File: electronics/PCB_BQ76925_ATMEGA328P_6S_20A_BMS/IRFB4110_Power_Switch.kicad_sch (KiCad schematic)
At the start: 25 parts, among them Q1 IRFB4110, Q2 IRFB4110, Q3 IRFB4110, Q4 IRFB4110, Q5 BC817, U2 LMR50410

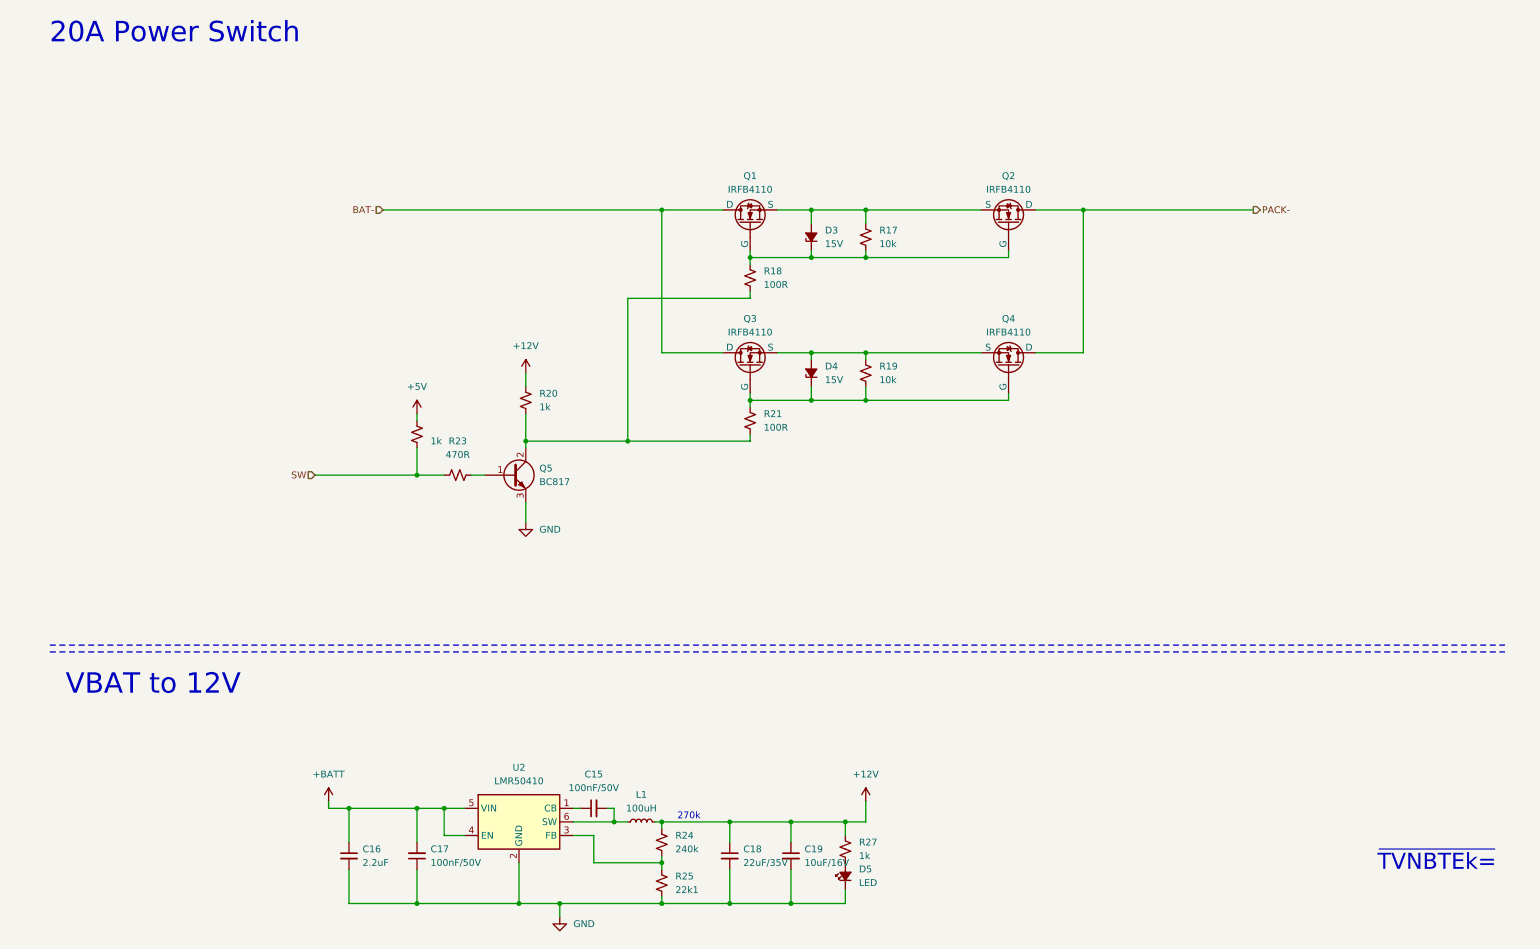
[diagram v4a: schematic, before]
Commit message: schematic components footprint updated
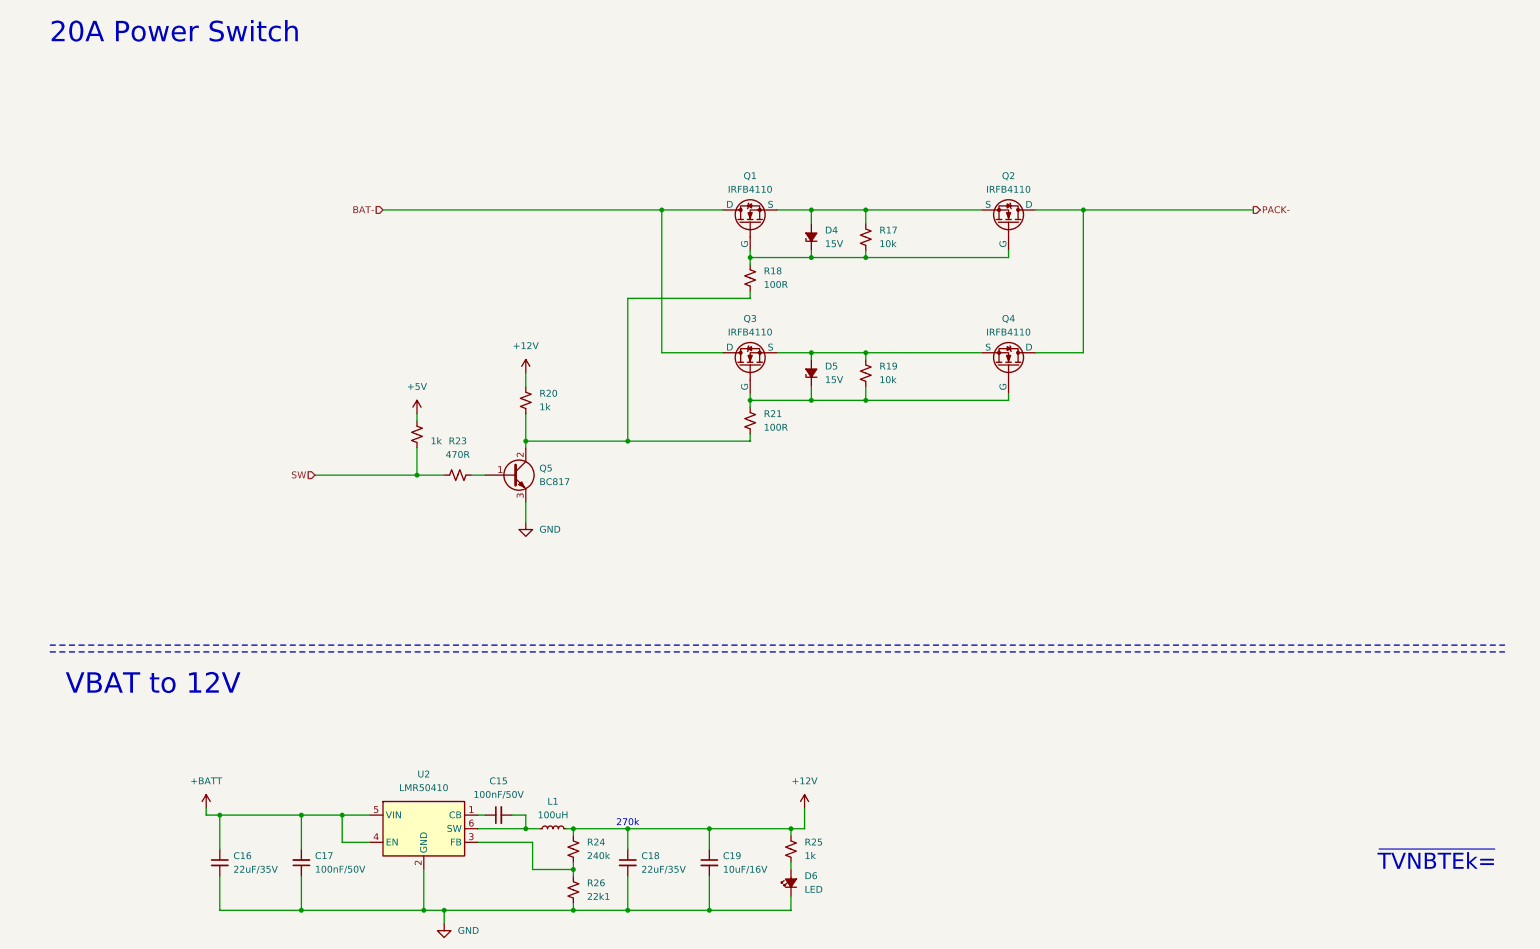
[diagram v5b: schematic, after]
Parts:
- removed Q1, Q2, Q3, Q4: IRFB4110, symbol BQ76925_ATMEGA328P_6S_20A_BMS:NMOS_1
- added Q1, Q2, Q3, Q4: IRFB4110, Package_TO_SOT_THT:TO-220-3_Horizontal_TabDown, symbol BQ76925_ATMEGA328P_6S_20A_BMS:NMOS
- C16: value 2.2uF -> 22uF/35V; footprint (none) -> Capacitor_SMD:CP_Elec_6.3x5.7
- D4: renamed from D3; footprint (none) -> Diode_SMD:D_SOD-123
- D5: renamed from D4; footprint (none) -> Diode_SMD:D_SOD-123
- D6: renamed from D5; symbol Device:LED_Small_Filled -> BQ76925_ATMEGA328P_6S_20A_BMS:LED_Small_Filled
- renumbered R27 to R25, R25 to R26
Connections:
- net BAT-: now also Q1.2 (D), Q3.2 (D)
- net PACK-: now also Q2.2 (D), Q4.2 (D)
- net at D4.1 (K), R17.1, R18.1: now also Q1.1 (G), Q2.1 (G)
- net at D4.2 (A), R17.2: now also Q1.3 (S), Q2.3 (S)
- net at D5.1 (K), R19.1, R21.1: now also Q3.1 (G), Q4.1 (G)
- net at D5.2 (A), R19.2: now also Q3.3 (S), Q4.3 (S)
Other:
- moved on the sheet: C15, C17, C18, C19, D6, L1, R24, R25, R26, U2

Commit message: pcb design half complete
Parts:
- added C18: 100nF/50V, Capacitor_SMD:C_0805_2012Metric_Pad1.18x1.45mm_HandSolder, symbol BQ76925_ATMEGA328P_6S_20A_BMS:C_Small
- renumbered C16 to C15, C17 to C16, C15 to C17, C18 to C19, C19 to C20, D6 to D4, D4 to D5, D5 to D6, Q5 to Q1, Q1 to Q2, Q2 to Q4, Q4 to Q5, R22 to R17, R23 to R18, R20 to R19, R24 to R20, R26 to R21, R18 to R22, R21 to R23, R25 to R24, R17 to R25, R19 to R26
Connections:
- net GND: now also C18.2
- net at Q1.2 (C), R19.1, R22.2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: now also C18.1

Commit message: PCB DRC complete footprints library exported. PCB optimization required
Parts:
- C15, C19: footprint Capacitor_SMD:CP_Elec_6.3x5.7 -> BQ76925_ATMEGA328P_6S_20A_BMS:CP_Elec_6.3x5.7
- C16, C17, C18: footprint Capacitor_SMD:C_0805_2012Metric_Pad1.18x1.45mm_HandSolder -> BQ76925_ATMEGA328P_6S_20A_BMS:C_0805_2012Metric_Pad1.18x1.45mm_HandSolder
- C20: footprint Capacitor_SMD:C_0603_1608Metric_Pad1.08x0.95mm_HandSolder -> BQ76925_ATMEGA328P_6S_20A_BMS:C_0603_1608Metric_Pad1.08x0.95mm_HandSolder
- D4, R20: footprint Resistor_SMD:R_0805_2012Metric_Pad1.20x1.40mm_HandSolder -> BQ76925_ATMEGA328P_6S_20A_BMS:R_0805_2012Metric_Pad1.20x1.40mm_HandSolder
- D5, D6: footprint Diode_SMD:D_SOD-123 -> BQ76925_ATMEGA328P_6S_20A_BMS:D_SOD-123
- L1: footprint Inductor_SMD:L_7.3x7.3_H3.5 -> BQ76925_ATMEGA328P_6S_20A_BMS:L_7.3x7.3_H3.5
- Q1: footprint Package_TO_SOT_SMD:SOT-23 -> BQ76925_ATMEGA328P_6S_20A_BMS:SOT-23
- Q2, Q3, Q4, Q5: footprint Package_TO_SOT_THT:TO-220-3_Horizontal_TabDown -> BQ76925_ATMEGA328P_6S_20A_BMS:TO-220-3_Horizontal_TabDown
- R17, R18, R19, R21, R24, R25, R26: footprint Resistor_SMD:R_0603_1608Metric_Pad0.98x0.95mm_HandSolder -> BQ76925_ATMEGA328P_6S_20A_BMS:R_0603_1608Metric_Pad0.98x0.95mm_HandSolder
- R22, R23: footprint Resistor_SMD:R_1206_3216Metric_Pad1.30x1.75mm_HandSolder -> BQ76925_ATMEGA328P_6S_20A_BMS:R_1206_3216Metric_Pad1.30x1.75mm_HandSolder
- U2: footprint Package_TO_SOT_SMD:SOT-23-6 -> BQ76925_ATMEGA328P_6S_20A_BMS:SOT-23-6
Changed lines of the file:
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@@
 			)
 		)
-		(property "Footprint" "Capacitor_SMD:C_0805_2012Metric_Pad1.18x1.45mm_HandSolder"
+		(property "Footprint" "BQ76925_ATMEGA328P_6S_20A_BMS:C_0805_2012Metric_Pad1.18x1.45mm_HandSolder"
 			(at 59.69 173.99 0)
 			(effects
@@
 			)
 		)
-		(property "Footprint" "Package_TO_SOT_THT:TO-220-3_Horizontal_TabDown"
+		(property "Footprint" "BQ76925_ATMEGA328P_6S_20A_BMS:TO-220-3_Horizontal_TabDown"
 			(at 200.406 77.216 0)
 			(effects
@@
 			)
 		)
-		(property "Footprint" "Capacitor_SMD:C_0805_2012Metric_Pad1.18x1.45mm_HandSolder"
+		(property "Footprint" "BQ76925_ATMEGA328P_6S_20A_BMS:C_0805_2012Metric_Pad1.18x1.45mm_HandSolder"
 			(at 96.52 165.1 0)
 			(effects
@@
 			)
 		)
-		(property "Footprint" "Package_TO_SOT_THT:TO-220-3_Horizontal_TabDown"
+		(property "Footprint" "BQ76925_ATMEGA328P_6S_20A_BMS:TO-220-3_Horizontal_TabDown"
 			(at 134.874 77.216 0)
 			(effects
@@
 			)
 		)
-		(property "Footprint" "Resistor_SMD:R_0603_1608Metric_Pad0.98x0.95mm_HandSolder"
+		(property "Footprint" "BQ76925_ATMEGA328P_6S_20A_BMS:R_0603_1608Metric_Pad0.98x0.95mm_HandSolder"
 			(at 110.49 179.07 0)
 			(effects
@@
 			)
 		)
-		(property "Footprint" "Resistor_SMD:R_0603_1608Metric_Pad0.98x0.95mm_HandSolder"
+		(property "Footprint" "BQ76925_ATMEGA328P_6S_20A_BMS:R_0603_1608Metric_Pad0.98x0.95mm_HandSolder"
 			(at 165.1 82.55 0)
 			(effects
@@
 			)
 		)
-		(property "Footprint" "Resistor_SMD:R_0805_2012Metric_Pad1.20x1.40mm_HandSolder"
+		(property "Footprint" "BQ76925_ATMEGA328P_6S_20A_BMS:R_0805_2012Metric_Pad1.20x1.40mm_HandSolder"
 			(at 110.49 171.45 0)
 			(effects
@@
 			)
 		)
-		(property "Footprint" "Capacitor_SMD:C_0603_1608Metric_Pad1.08x0.95mm_HandSolder"
+		(property "Footprint" "BQ76925_ATMEGA328P_6S_20A_BMS:C_0603_1608Metric_Pad1.08x0.95mm_HandSolder"
 			(at 135.89 173.99 0)
 			(effects
@@
 			)
 		)
-		(property "Footprint" "Resistor_SMD:R_0603_1608Metric_Pad0.98x0.95mm_HandSolder"
+		(property "Footprint" "BQ76925_ATMEGA328P_6S_20A_BMS:R_0603_1608Metric_Pad0.98x0.95mm_HandSolder"
 			(at 151.13 171.45 0)
 			(effects
@@
 			)
 		)
-		(property "Footprint" "Diode_SMD:D_SOD-123"
+		(property "Footprint" "BQ76925_ATMEGA328P_6S_20A_BMS:D_SOD-123"
 			(at 154.94 82.55 90)
 			(effects
@@
 			)
 		)
-		(property "Footprint" "Capacitor_SMD:C_0805_2012Metric_Pad1.18x1.45mm_HandSolder"
+		(property "Footprint" "BQ76925_ATMEGA328P_6S_20A_BMS:C_0805_2012Metric_Pad1.18x1.45mm_HandSolder"
 			(at 115.57 102.87 0)
 			(effects
@@
 			)
 		)
-		(property "Footprint" "Package_TO_SOT_SMD:SOT-23"
+		(property "Footprint" "BQ76925_ATMEGA328P_6S_20A_BMS:SOT-23"
 			(at 104.14 99.06 0)
 			(effects
@@
 			)
 		)
-		(property "Footprint" "Resistor_SMD:R_0603_1608Metric_Pad0.98x0.95mm_HandSolder"
+		(property "Footprint" "BQ76925_ATMEGA328P_6S_20A_BMS:R_0603_1608Metric_Pad0.98x0.95mm_HandSolder"
 			(at 81.28 93.98 0)
 			(effects
@@
 			)
 		)
-		(property "Footprint" "Package_TO_SOT_SMD:SOT-23-6"
+		(property "Footprint" "BQ76925_ATMEGA328P_6S_20A_BMS:SOT-23-6"
 			(at 83.82 176.53 0)
 			(effects
@@
 			)
 		)
-		(property "Footprint" "Resistor_SMD:R_0603_1608Metric_Pad0.98x0.95mm_HandSolder"
+		(property "Footprint" "BQ76925_ATMEGA328P_6S_20A_BMS:R_0603_1608Metric_Pad0.98x0.95mm_HandSolder"
 			(at 165.1 57.15 0)
 			(effects
@@
 			)
 		)
-		(property "Footprint" "Resistor_SMD:R_1206_3216Metric_Pad1.30x1.75mm_HandSolder"
+		(property "Footprint" "BQ76925_ATMEGA328P_6S_20A_BMS:R_1206_3216Metric_Pad1.30x1.75mm_HandSolder"
 			(at 143.51 91.44 0)
 			(effects
@@
 			)
 		)
-		(property "Footprint" "Capacitor_SMD:CP_Elec_6.3x5.7"
+		(property "Footprint" "BQ76925_ATMEGA328P_6S_20A_BMS:CP_Elec_6.3x5.7"
 			(at 44.45 173.99 0)
 			(effects
@@
 			)
 		)
-		(property "Footprint" "Capacitor_SMD:CP_Elec_6.3x5.7"
+		(property "Footprint" "BQ76925_ATMEGA328P_6S_20A_BMS:CP_Elec_6.3x5.7"
 			(at 120.65 173.99 0)
 			(effects
@@
 			)
 		)
-		(property "Footprint" "Package_TO_SOT_THT:TO-220-3_Horizontal_TabDown"
+		(property "Footprint" "BQ76925_ATMEGA328P_6S_20A_BMS:TO-220-3_Horizontal_TabDown"
 			(at 200.406 50.546 0)
 			(effects
@@
 			)
 		)
-		(property "Footprint" "Inductor_SMD:L_7.3x7.3_H3.5"
+		(property "Footprint" "BQ76925_ATMEGA328P_6S_20A_BMS:L_7.3x7.3_H3.5"
 			(at 106.68 167.64 0)
 			(effects
@@
 			)
 		)
-		(property "Footprint" "Diode_SMD:D_SOD-123"
+		(property "Footprint" "BQ76925_ATMEGA328P_6S_20A_BMS:D_SOD-123"
 			(at 154.94 57.15 90)
 			(effects
@@
 			)
 		)
-		(property "Footprint" "Resistor_SMD:R_0805_2012Metric_Pad1.20x1.40mm_HandSolder"
+		(property "Footprint" "BQ76925_ATMEGA328P_6S_20A_BMS:R_0805_2012Metric_Pad1.20x1.40mm_HandSolder"
 			(at 151.13 177.8 90)
 			(effects
@@
 			)
 		)
-		(property "Footprint" "Package_TO_SOT_THT:TO-220-3_Horizontal_TabDown"
+		(property "Footprint" "BQ76925_ATMEGA328P_6S_20A_BMS:TO-220-3_Horizontal_TabDown"
 			(at 134.874 50.546 0)
 			(effects
@@
 			)
 		)
-		(property "Footprint" "Resistor_SMD:R_0603_1608Metric_Pad0.98x0.95mm_HandSolder"
+		(property "Footprint" "BQ76925_ATMEGA328P_6S_20A_BMS:R_0603_1608Metric_Pad0.98x0.95mm_HandSolder"
 			(at 101.6 87.63 0)
 			(effects
@@
 			)
 		)
-		(property "Footprint" "Resistor_SMD:R_1206_3216Metric_Pad1.30x1.75mm_HandSolder"
+		(property "Footprint" "BQ76925_ATMEGA328P_6S_20A_BMS:R_1206_3216Metric_Pad1.30x1.75mm_HandSolder"
 			(at 143.51 64.77 0)
 			(effects
@@
 			)
 		)
-		(property "Footprint" "Resistor_SMD:R_0603_1608Metric_Pad0.98x0.95mm_HandSolder"
+		(property "Footprint" "BQ76925_ATMEGA328P_6S_20A_BMS:R_0603_1608Metric_Pad0.98x0.95mm_HandSolder"
 			(at 88.9 101.6 0)
 			(effects
